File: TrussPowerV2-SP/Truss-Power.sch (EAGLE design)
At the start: 20 parts, among them J1 XF2L-0535-1, U2 MCP73831T-2ACI/OT, U3 MAX17044, X1 22-23-2021, X2 MicroB, X3 22-23-2021

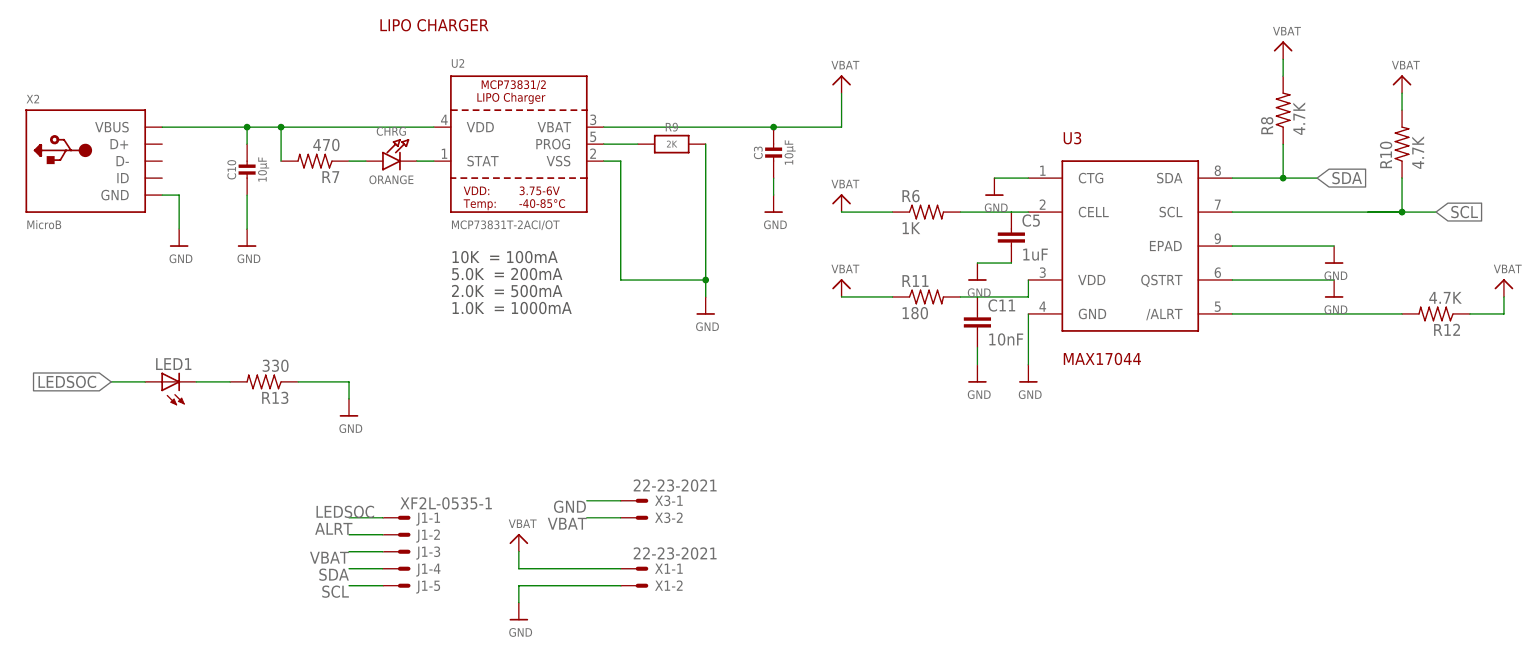
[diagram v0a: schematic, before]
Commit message: VBAT Polygon
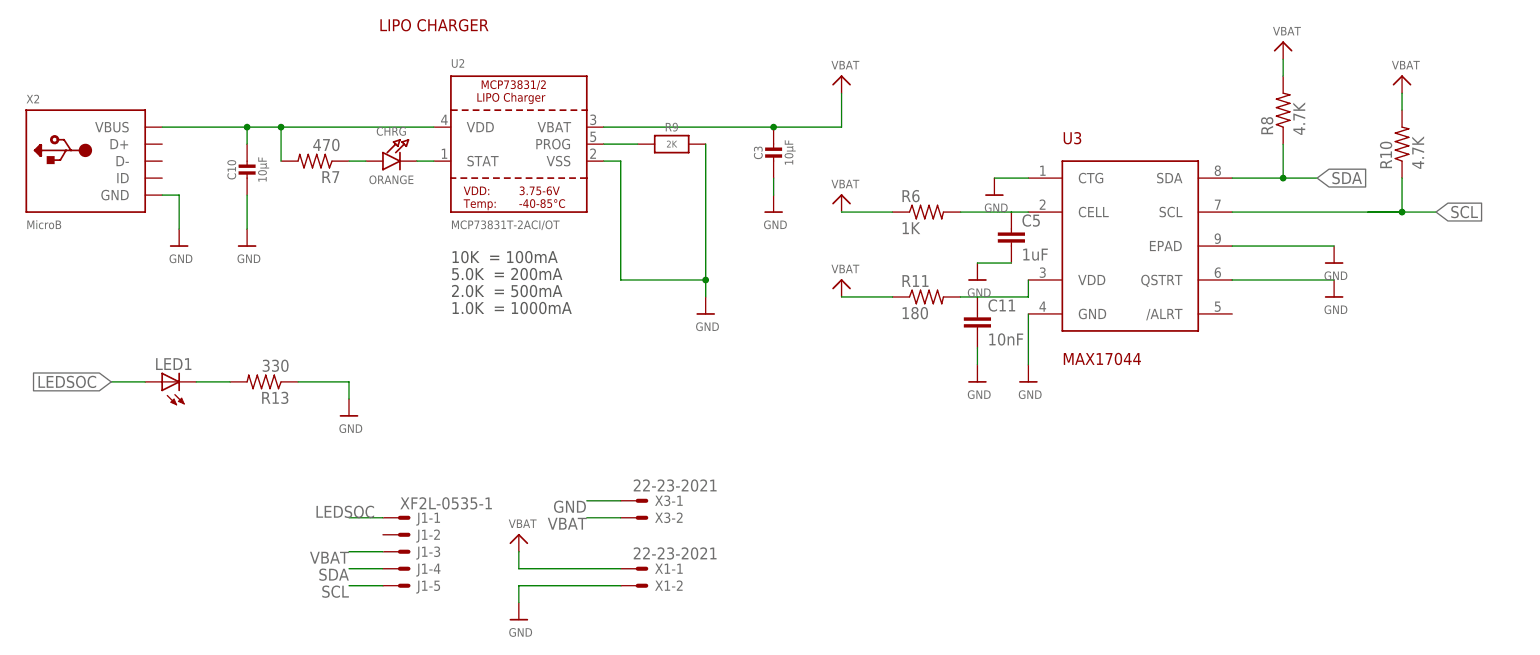
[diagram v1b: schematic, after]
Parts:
- removed R12: 4.7K, resistor:R-US_R0402
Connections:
- removed net ALRT: J1-2.MS, R12.2, U3./ALRT
- net VBAT: no longer R12.1
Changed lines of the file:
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@@
 <?xml version="1.0" encoding="utf-8"?>
 <!DOCTYPE eagle SYSTEM "eagle.dtd">
-<eagle version="9.2.2">
+<eagle version="9.1.3">
 <drawing>
 <settings>
@@
 <part name="U$4" library="microbuilder" deviceset="GND" device=""/>
 <part name="U$19" library="microbuilder" deviceset="GND" device=""/>
-<part name="R12" library="resistor" deviceset="R-US_" device="R0402" value="4.7K"/>
 <part name="C5" library="rcl" deviceset="C-EU" device="C0603" value="1uF"/>
 <part name="U$20" library="microbuilder" deviceset="GND" device=""/>
@@
 <part name="U$9" library="microbuilder" deviceset="VBAT" device=""/>
 <part name="U$10" library="microbuilder" deviceset="VBAT" device=""/>
-<part name="U$11" library="microbuilder" deviceset="VBAT" device=""/>
 </parts>
 <sheets>
@@
 <attribute name="VALUE" x="201.676" y="53.34" size="1.27" layer="96"/>
 </instance>
-<instance part="R12" gate="G$1" x="218.44" y="53.34" smashed="yes" rot="R180">
-<attribute name="NAME" x="222.25" y="51.8414" size="1.778" layer="95" rot="R180"/>
-<attribute name="VALUE" x="222.25" y="56.642" size="1.778" layer="96" rot="R180"/>
-</instance>
 <instance part="C5" gate="G$1" x="154.94" y="66.04" smashed="yes">
 <attribute name="NAME" x="156.464" y="66.421" size="1.778" layer="95"/>
@@
 <instance part="U$10" gate="G$1" x="213.36" y="88.9" smashed="yes">
 <attribute name="VALUE" x="211.836" y="89.916" size="1.27" layer="96"/>
-</instance>
-<instance part="U$11" gate="G$1" x="228.6" y="58.42" smashed="yes">
-<attribute name="VALUE" x="227.076" y="59.436" size="1.27" layer="96"/>
 </instance>
 </instances>
@@
 <pinref part="U$10" gate="G$1" pin="VBAT"/>
 <wire x1="213.36" y1="83.82" x2="213.36" y2="86.36" width="0.1524" layer="91"/>
-</segment>
-<segment>
-<pinref part="R12" gate="G$1" pin="1"/>
-<pinref part="U$11" gate="G$1" pin="VBAT"/>
-<wire x1="223.52" y1="53.34" x2="228.6" y2="53.34" width="0.1524" layer="91"/>
-<wire x1="228.6" y1="53.34" x2="228.6" y2="55.88" width="0.1524" layer="91"/>
 </segment>
 <segment>
@@
 </segment>
 </net>
-<net name="ALRT" class="0">
-<segment>
-<pinref part="U3" gate="G$1" pin="/ALRT"/>
-<pinref part="R12" gate="G$1" pin="2"/>
-<wire x1="187.96" y1="53.34" x2="213.36" y2="53.34" width="0.1524" layer="91"/>
-</segment>
-<segment>
-<pinref part="J1" gate="-2" pin="MS"/>
-<wire x1="60.96" y1="20.32" x2="55.88" y2="20.32" width="0.1524" layer="91"/>
-<label x="50.8" y="20.32" size="1.778" layer="95"/>
-</segment>
-</net>

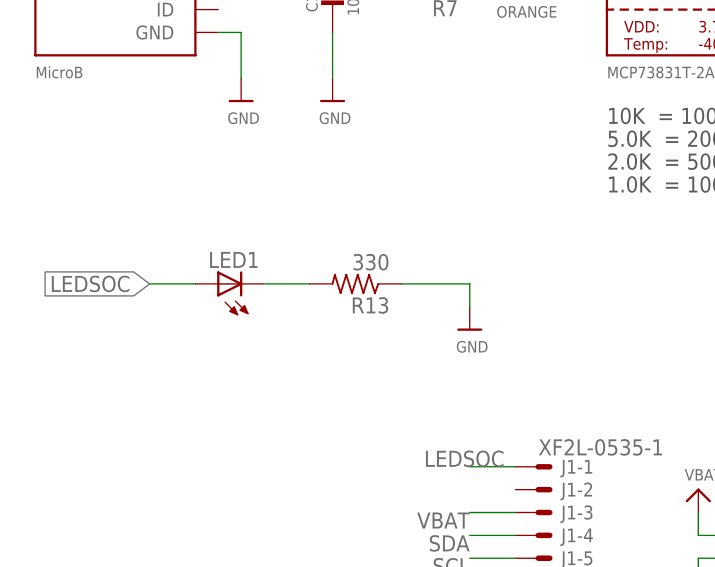
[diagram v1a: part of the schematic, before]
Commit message: LED moved
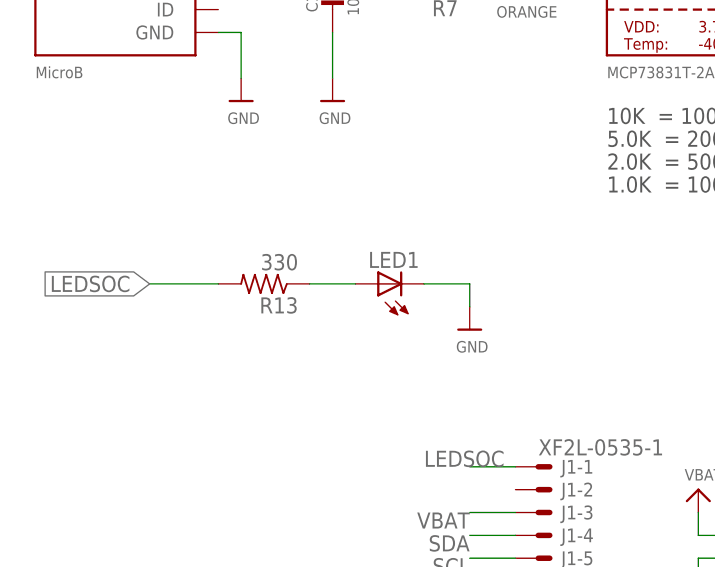
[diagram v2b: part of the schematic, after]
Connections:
- net GND: now also LED1.C; no longer R13.1
- net LEDSOC: now also R13.2; no longer LED1.A
- net N$4: now also LED1.A, R13.1; no longer LED1.C, R13.2
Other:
- moved on the sheet: LED1, R13
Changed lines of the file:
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@@
 <?xml version="1.0" encoding="utf-8"?>
 <!DOCTYPE eagle SYSTEM "eagle.dtd">
-<eagle version="9.1.3">
+<eagle version="9.2.2">
 <drawing>
 <settings>
@@
 <attribute name="VALUE" x="128.016" y="72.136" size="1.27" layer="96"/>
 </instance>
-<instance part="LED1" gate="G$1" x="27.94" y="43.18" smashed="yes" rot="R90">
-<attribute name="NAME" x="32.512" y="46.736" size="1.778" layer="95" rot="R180"/>
-<attribute name="VALUE" x="32.512" y="48.895" size="1.778" layer="96" rot="R180"/>
-</instance>
-<instance part="R13" gate="G$1" x="43.18" y="43.18" smashed="yes" rot="R180">
-<attribute name="NAME" x="46.99" y="41.6814" size="1.778" layer="95" rot="R180"/>
-<attribute name="VALUE" x="46.99" y="46.482" size="1.778" layer="96" rot="R180"/>
+<instance part="LED1" gate="G$1" x="45.72" y="43.18" smashed="yes" rot="R90">
+<attribute name="NAME" x="50.292" y="46.736" size="1.778" layer="95" rot="R180"/>
+<attribute name="VALUE" x="50.292" y="48.895" size="1.778" layer="96" rot="R180"/>
+</instance>
+<instance part="R13" gate="G$1" x="33.02" y="43.18" smashed="yes" rot="R180">
+<attribute name="NAME" x="36.83" y="41.6814" size="1.778" layer="95" rot="R180"/>
+<attribute name="VALUE" x="36.83" y="46.482" size="1.778" layer="96" rot="R180"/>
 </instance>
 <instance part="U$22" gate="G$1" x="55.88" y="38.1" smashed="yes">
@@
 </segment>
 <segment>
-<pinref part="R13" gate="G$1" pin="1"/>
 <pinref part="U$22" gate="G$1" pin="GND"/>
-<wire x1="48.26" y1="43.18" x2="55.88" y2="43.18" width="0.1524" layer="91"/>
 <wire x1="55.88" y1="43.18" x2="55.88" y2="40.64" width="0.1524" layer="91"/>
+<pinref part="LED1" gate="G$1" pin="C"/>
+<wire x1="55.88" y1="43.18" x2="50.8" y2="43.18" width="0.1524" layer="91"/>
 </segment>
 </net>
@@
 </segment>
 <segment>
-<wire x1="25.4" y1="43.18" x2="20.32" y2="43.18" width="0.1524" layer="91"/>
+<pinref part="R13" gate="G$1" pin="2"/>
+<wire x1="27.94" y1="43.18" x2="20.32" y2="43.18" width="0.1524" layer="91"/>
 <label x="20.32" y="43.18" size="1.778" layer="95" rot="R180" xref="yes"/>
-<pinref part="LED1" gate="G$1" pin="A"/>
-</segment>
-</net>
-<net name="N$4" class="0">
-<segment>
-<pinref part="LED1" gate="G$1" pin="C"/>
-<pinref part="R13" gate="G$1" pin="2"/>
-<wire x1="33.02" y1="43.18" x2="38.1" y2="43.18" width="0.1524" layer="91"/>
 </segment>
 </net>
@@
 </segment>
 </net>
+<net name="N$4" class="0">
+<segment>
+<pinref part="LED1" gate="G$1" pin="A"/>
+<pinref part="R13" gate="G$1" pin="1"/>
+<wire x1="43.18" y1="43.18" x2="38.1" y2="43.18" width="0.1524" layer="91"/>
+</segment>
+</net>
